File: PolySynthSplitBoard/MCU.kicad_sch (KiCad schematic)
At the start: 101 parts, among them J401 PWR, J402 DATA, J403 SWD Header, J404 MIDI_In, J405 Micro_SD_Card_Det2, J406 MIDI_Out, J407 MIDI_Thru, SW401 RST, SW402 BOOT, U401 STM32F411RETx, U402 74HC595, U403 74HC595, U404 74HC04, U405 6N138, Y401 16MHz, Y402 32.768kHZ

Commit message: voice rev4 passing DRC
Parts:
- added R447: LOOP, Resistor_THT:R_Axial_DIN0204_L3.6mm_D1.6mm_P5.08mm_Horizontal, symbol Device:R_US
- added TP421: INTR_A, TestPoint:TestPoint_THTPad_D1.0mm_Drill0.5mm_VAL, symbol Connector:TestPoint
- added TP422: INTR_B, TestPoint:TestPoint_THTPad_D1.0mm_Drill0.5mm_VAL, symbol Connector:TestPoint
- added TP423: INTR_C, TestPoint:TestPoint_THTPad_D1.0mm_Drill0.5mm_VAL, symbol Connector:TestPoint
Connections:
- net EXP_INTR_A: now also TP421.1
- net EXP_INTR_B: now also TP422.1
- net EXP_INTR_C: now also TP423.1
- net GND: now also R447.1, R447.2
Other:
- moved on the sheet: R446, TP418, TP419, TP420

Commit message: mod matrix logic stuff
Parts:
- TP401: value MUX_INH -> TestPoint; now left out of the parts list
- TP402: value MUX_A0 -> TestPoint; now left out of the parts list
- TP403: value MUX_A1 -> TestPoint; now left out of the parts list
- TP404: value MUX_A2 -> TestPoint; now left out of the parts list
- TP405: value HP_MODE -> TestPoint; now left out of the parts list
- TP406: value FOLD_FIRST -> TestPoint; now left out of the parts list
- TP407: value EXP_CS -> TestPoint; now left out of the parts list
- TP408: value EXP_SCK -> TestPoint; now left out of the parts list
- TP409: value EXP_MISO -> TestPoint; now left out of the parts list
- TP410: value EXP_MOSI -> TestPoint; now left out of the parts list
- TP411: value CLK_CS -> TestPoint; now left out of the parts list
- TP412: value CLK_SCK -> TestPoint; now left out of the parts list
- TP413: value CLK_MOSI -> TestPoint; now left out of the parts list
- TP414: value MIDI_RX -> TestPoint; now left out of the parts list
- TP415: value MIDI_TX -> TestPoint; now left out of the parts list
- TP416: value POTS_SCL -> TestPoint; now left out of the parts list
- TP417: value POTS_SDA -> TestPoint; now left out of the parts list
- TP418: value DAC_SCL -> TestPoint; now left out of the parts list
- TP419: value DAC_SDA -> TestPoint; now left out of the parts list
- TP420: value LDAC -> TestPoint; now left out of the parts list
- TP421: value INTR_A -> TestPoint; now left out of the parts list
- TP422: value INTR_B -> TestPoint; now left out of the parts list
- TP423: value INTR_C -> TestPoint; now left out of the parts list
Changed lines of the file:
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@@
 		(unit 1)
 		(exclude_from_sim no)
-		(in_bom yes)
+		(in_bom no)
 		(on_board yes)
 		(dnp no)
 		(fields_autoplaced yes)
 		(property "Reference" "TP403"
-			(at 83.058 236.4739 0)
+			(at 82.55 236.4739 0)
 			(effects
 				(font
@@
 			)
 		)
-		(property "Value" "MUX_A1"
-			(at 83.058 239.0139 0)
+		(property "Value" "TestPoint"
+			(at 82.55 239.0139 0)
 			(effects
 				(font
@@
 		(unit 1)
 		(exclude_from_sim no)
-		(in_bom yes)
+		(in_bom no)
 		(on_board yes)
 		(dnp no)
 		(fields_autoplaced yes)
 		(property "Reference" "TP423"
-			(at 188.722 247.3959 0)
+			(at 187.96 247.3959 0)
 			(effects
 				(font
@@
 			)
 		)
-		(property "Value" "INTR_C"
-			(at 188.722 249.9359 0)
+		(property "Value" "TestPoint"
+			(at 187.96 249.9359 0)
 			(effects
 				(font
@@
 		(unit 1)
 		(exclude_from_sim no)
-		(in_bom yes)
+		(in_bom no)
 		(on_board yes)
 		(dnp no)
 		(fields_autoplaced yes)
 		(property "Reference" "TP402"
-			(at 83.058 228.8539 0)
+			(at 83.82 228.8539 0)
 			(effects
 				(font
@@
 			)
 		)
-		(property "Value" "MUX_A0"
-			(at 83.058 231.3939 0)
+		(property "Value" "TestPoint"
+			(at 83.82 231.3939 0)
 			(effects
 				(font
@@
 		(unit 1)
 		(exclude_from_sim no)
-		(in_bom yes)
+		(in_bom no)
 		(on_board yes)
 		(dnp no)
@@
 			)
 		)
-		(property "Value" "EXP_SCK"
+		(property "Value" "TestPoint"
 			(at 118.11 242.5699 0)
 			(effects
@@
 		(unit 1)
 		(exclude_from_sim no)
-		(in_bom yes)
+		(in_bom no)
 		(on_board yes)
 		(dnp no)
 		(fields_autoplaced yes)
 		(property "Reference" "TP420"
-			(at 172.466 226.8219 0)
+			(at 172.72 226.8219 0)
 			(effects
 				(font
@@
 			)
 		)
-		(property "Value" "LDAC"
-			(at 172.466 229.3619 0)
+		(property "Value" "TestPoint"
+			(at 172.72 229.3619 0)
 			(effects
 				(font
@@
 		(unit 1)
 		(exclude_from_sim no)
-		(in_bom yes)
+		(in_bom no)
 		(on_board yes)
 		(dnp no)
 		(fields_autoplaced yes)
 		(property "Reference" "TP406"
-			(at 83.058 262.3819 0)
+			(at 83.82 262.3819 0)
 			(effects
 				(font
@@
 			)
 		)
-		(property "Value" "FOLD_FIRST"
-			(at 83.058 264.9219 0)
+		(property "Value" "TestPoint"
+			(at 83.82 264.9219 0)
 			(effects
 				(font
@@
 		(unit 1)
 		(exclude_from_sim no)
-		(in_bom yes)
+		(in_bom no)
 		(on_board yes)
 		(dnp no)
 		(fields_autoplaced yes)
 		(property "Reference" "TP422"
-			(at 187.452 235.4579 0)
+			(at 187.96 235.4579 0)
 			(effects
 				(font
@@
 			)
 		)
-		(property "Value" "INTR_B"
-			(at 187.452 237.9979 0)
+		(property "Value" "TestPoint"
+			(at 187.96 237.9979 0)
 			(effects
 				(font
@@
 		(unit 1)
 		(exclude_from_sim no)
-		(in_bom yes)
+		(in_bom no)
 		(on_board yes)
 		(dnp no)
 		(fields_autoplaced yes)
 		(property "Reference" "TP401"
-			(at 83.058 221.2339 0)
+			(at 83.82 221.2339 0)
 			(effects
 				(font
@@
 			)
 		)
-		(property "Value" "MUX_INH"
-			(at 83.058 223.7739 0)
+		(property "Value" "TestPoint"
+			(at 83.82 223.7739 0)
 			(effects
 				(font
@@
 		(unit 1)
 		(exclude_from_sim no)
-		(in_bom yes)
+		(in_bom no)
 		(on_board yes)
 		(dnp no)
 		(fields_autoplaced yes)
 		(property "Reference" "TP405"
-			(at 84.328 253.7459 0)
+			(at 83.82 253.7459 0)
 			(effects
 				(font
@@
 			)
 		)
-		(property "Value" "HP_MODE"
-			(at 84.328 256.2859 0)
+		(property "Value" "TestPoint"
+			(at 83.82 256.2859 0)
 			(effects
 				(font
@@
 		(unit 1)
 		(exclude_from_sim no)
-		(in_bom yes)
+		(in_bom no)
 		(on_board yes)
 		(dnp no)
@@
 			)
 		)
-		(property "Value" "POTS_SDA"
+		(property "Value" "TestPoint"
 			(at 154.94 227.5839 0)
 			(effects
@@
 		(unit 1)
 		(exclude_from_sim no)
-		(in_bom yes)
+		(in_bom no)
 		(on_board yes)
 		(dnp no)
@@
 			)
 		)
-		(property "Value" "EXP_MISO"
+		(property "Value" "TestPoint"
 			(at 118.11 252.4759 0)
 			(effects
@@
 		(unit 1)
 		(exclude_from_sim no)
-		(in_bom yes)
+		(in_bom no)
 		(on_board yes)
 		(dnp no)
 		(fields_autoplaced yes)
 		(property "Reference" "TP419"
-			(at 172.466 248.1579 0)
+			(at 172.72 248.1579 0)
 			(effects
 				(font
@@
 			)
 		)
-		(property "Value" "DAC_SDA"
-			(at 172.466 250.6979 0)
+		(property "Value" "TestPoint"
+			(at 172.72 250.6979 0)
 			(effects
 				(font
@@
 		(unit 1)
 		(exclude_from_sim no)
-		(in_bom yes)
+		(in_bom no)
 		(on_board yes)
 		(dnp no)
 		(fields_autoplaced yes)
 		(property "Reference" "TP413"
-			(at 137.922 257.5559 0)
+			(at 138.43 257.5559 0)
 			(effects
 				(font
@@
 			)
 		)
-		(property "Value" "CLK_MOSI"
-			(at 137.922 260.0959 0)
+		(property "Value" "TestPoint"
+			(at 138.43 260.0959 0)
 			(effects
 				(font
@@
 		(unit 1)
 		(exclude_from_sim no)
-		(in_bom yes)
+		(in_bom no)
 		(on_board yes)
 		(dnp no)
 		(fields_autoplaced yes)
 		(property "Reference" "TP421"
-			(at 187.452 219.9639 0)
+			(at 187.96 219.9639 0)
 			(effects
 				(font
@@
 			)
 		)
-		(property "Value" "INTR_A"
-			(at 187.452 222.5039 0)
+		(property "Value" "TestPoint"
+			(at 187.96 222.5039 0)
 			(effects
 				(font
@@
 		(unit 1)
 		(exclude_from_sim no)
-		(in_bom yes)
+		(in_bom no)
 		(on_board yes)
 		(dnp no)
 		(fields_autoplaced yes)
 		(property "Reference" "TP412"
-			(at 137.922 245.8719 0)
+			(at 138.43 245.8719 0)
 			(effects
 				(font
@@
 			)
 		)
-		(property "Value" "CLK_SCK"
-			(at 137.922 248.4119 0)
+		(property "Value" "TestPoint"
+			(at 138.43 248.4119 0)
 			(effects
 				(font
@@
 		(unit 1)
 		(exclude_from_sim no)
-		(in_bom yes)
+		(in_bom no)
 		(on_board yes)
 		(dnp no)
@@
 			)
 		)
-		(property "Value" "EXP_CS"
+		(property "Value" "TestPoint"
 			(at 118.11 232.9179 0)
 			(effects
@@
 		(unit 1)
 		(exclude_from_sim no)
-		(in_bom yes)
+		(in_bom no)
 		(on_board yes)
 		(dnp no)
 		(fields_autoplaced yes)
 		(property "Reference" "TP404"
-			(at 83.058 244.6019 0)
+			(at 83.82 244.6019 0)
 			(effects
 				(font
@@
 			)
 		)
-		(property "Value" "MUX_A2"
-			(at 83.058 247.1419 0)
+		(property "Value" "TestPoint"
+			(at 83.82 247.1419 0)
 			(effects
 				(font
@@
 		(unit 1)
 		(exclude_from_sim no)
-		(in_bom yes)
+		(in_bom no)
 		(on_board yes)
 		(dnp no)
 		(fields_autoplaced yes)
 		(property "Reference" "TP411"
-			(at 137.922 236.4739 0)
+			(at 137.16 236.4739 0)
 			(effects
 				(font
@@
 			)
 		)
-		(property "Value" "CLK_CS"
-			(at 137.922 239.0139 0)
+		(property "Value" "TestPoint"
+			(at 137.16 239.0139 0)
 			(effects
 				(font
@@
 		(unit 1)
 		(exclude_from_sim no)
-		(in_bom yes)
+		(in_bom no)
 		(on_board yes)
 		(dnp no)
@@
 			)
 		)
-		(property "Value" "EXP_MOSI"
+		(property "Value" "TestPoint"
 			(at 118.11 262.3819 0)
 			(effects
@@
 		(unit 1)
 		(exclude_from_sim no)
-		(in_bom yes)
+		(in_bom no)
 		(on_board yes)
 		(dnp no)
@@
 			)
 		)
-		(property "Value" "MIDI_TX"
+		(property "Value" "TestPoint"
 			(at 137.16 227.8379 0)
 			(effects
@@
 		(unit 1)
 		(exclude_from_sim no)
-		(in_bom yes)
+		(in_bom no)
 		(on_board yes)
 		(dnp no)
@@
 			)
 		)
-		(property "Value" "POTS_SCL"
+		(property "Value" "TestPoint"
 			(at 153.67 217.9319 0)
 			(effects
@@
 		(unit 1)
 		(exclude_from_sim no)
-		(in_bom yes)
+		(in_bom no)
 		(on_board yes)
 		(dnp no)
 		(fields_autoplaced yes)
 		(property "Reference" "TP418"
-			(at 172.466 237.4899 0)
+			(at 172.72 237.4899 0)
 			(effects
 				(font
@@
 			)
 		)
-		(property "Value" "DAC_SCL"
-			(at 172.466 240.0299 0)
+		(property "Value" "TestPoint"
+			(at 172.72 240.0299 0)
 			(effects
 				(font
@@
 		(unit 1)
 		(exclude_from_sim no)
-		(in_bom yes)
+		(in_bom no)
 		(on_board yes)
 		(dnp no)
@@
 			)
 		)
-		(property "Value" "MIDI_RX"
+		(property "Value" "TestPoint"
 			(at 137.16 217.6779 0)
 			(effects

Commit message: motherboard rev2 passing DRC
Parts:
- TP401: value TestPoint -> MUX_INH
- TP402: value TestPoint -> MUX_A0
- TP403: value TestPoint -> MUX_A1
- TP404: value TestPoint -> MUX_A2
- TP405: value TestPoint -> HP_MODE
- TP406: value TestPoint -> FF
- TP407: value TestPoint -> EXP_CS
- TP408: value TestPoint -> EXP_SCK
- TP409: value TestPoint -> EXP_MISO
- TP410: value TestPoint -> EXP_MOSI
- TP411: value TestPoint -> PITCH_SS
- TP412: value TestPoint -> PITCH_SCK
- TP413: value TestPoint -> PITCH_MOSI
- TP414: value TestPoint -> MIDI_R
- TP415: value TestPoint -> MIDI_T
- TP416: value TestPoint -> POTS_SCL
- TP417: value TestPoint -> POTS_SDA
- TP418: value TestPoint -> DAC_SCL
- TP419: value TestPoint -> DAC_SDA
- TP420: value TestPoint -> LDAC
- TP421: value TestPoint -> EXP_INTA
- TP422: value TestPoint -> EXP_INTB
- TP423: value TestPoint -> EXP_INTC
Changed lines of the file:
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@@
 			)
 		)
-		(property "Value" "TestPoint"
+		(property "Value" "MUX_A1"
 			(at 82.55 239.0139 0)
 			(effects
@@
 			)
 		)
-		(property "Value" "TestPoint"
+		(property "Value" "EXP_INTC"
 			(at 187.96 249.9359 0)
 			(effects
@@
 			)
 		)
-		(property "Value" "TestPoint"
+		(property "Value" "MUX_A0"
 			(at 83.82 231.3939 0)
 			(effects
@@
 			)
 		)
-		(property "Value" "TestPoint"
+		(property "Value" "EXP_SCK"
 			(at 118.11 242.5699 0)
 			(effects
@@
 			)
 		)
-		(property "Value" "TestPoint"
+		(property "Value" "LDAC"
 			(at 172.72 229.3619 0)
 			(effects
@@
 			)
 		)
-		(property "Value" "TestPoint"
+		(property "Value" "FF"
 			(at 83.82 264.9219 0)
 			(effects
@@
 			)
 		)
-		(property "Value" "TestPoint"
+		(property "Value" "EXP_INTB"
 			(at 187.96 237.9979 0)
 			(effects
@@
 			)
 		)
-		(property "Value" "TestPoint"
+		(property "Value" "MUX_INH"
 			(at 83.82 223.7739 0)
 			(effects
@@
 			)
 		)
-		(property "Value" "TestPoint"
+		(property "Value" "HP_MODE"
 			(at 83.82 256.2859 0)
 			(effects
@@
 			)
 		)
-		(property "Value" "TestPoint"
+		(property "Value" "POTS_SDA"
 			(at 154.94 227.5839 0)
 			(effects
@@
 			)
 		)
-		(property "Value" "TestPoint"
+		(property "Value" "EXP_MISO"
 			(at 118.11 252.4759 0)
 			(effects
@@
 			)
 		)
-		(property "Value" "TestPoint"
+		(property "Value" "DAC_SDA"
 			(at 172.72 250.6979 0)
 			(effects
@@
 			)
 		)
-		(property "Value" "TestPoint"
+		(property "Value" "PITCH_MOSI"
 			(at 138.43 260.0959 0)
 			(effects
@@
 			)
 		)
-		(property "Value" "TestPoint"
+		(property "Value" "EXP_INTA"
 			(at 187.96 222.5039 0)
 			(effects
@@
 			)
 		)
-		(property "Value" "TestPoint"
+		(property "Value" "PITCH_SCK"
 			(at 138.43 248.4119 0)
 			(effects
@@
 			)
 		)
-		(property "Value" "TestPoint"
+		(property "Value" "EXP_CS"
 			(at 118.11 232.9179 0)
 			(effects
@@
 			)
 		)
-		(property "Value" "TestPoint"
+		(property "Value" "MUX_A2"
 			(at 83.82 247.1419 0)
 			(effects
@@
 			)
 		)
-		(property "Value" "TestPoint"
+		(property "Value" "PITCH_SS"
 			(at 137.16 239.0139 0)
 			(effects
@@
 			)
 		)
-		(property "Value" "TestPoint"
+		(property "Value" "EXP_MOSI"
 			(at 118.11 262.3819 0)
 			(effects
@@
 			)
 		)
-		(property "Value" "TestPoint"
+		(property "Value" "MIDI_T"
 			(at 137.16 227.8379 0)
 			(effects
@@
 			)
 		)
-		(property "Value" "TestPoint"
+		(property "Value" "POTS_SCL"
 			(at 153.67 217.9319 0)
 			(effects
@@
 			)
 		)
-		(property "Value" "TestPoint"
+		(property "Value" "DAC_SCL"
 			(at 172.72 240.0299 0)
 			(effects
@@
 			)
 		)
-		(property "Value" "TestPoint"
+		(property "Value" "MIDI_R"
 			(at 137.16 217.6779 0)
 			(effects

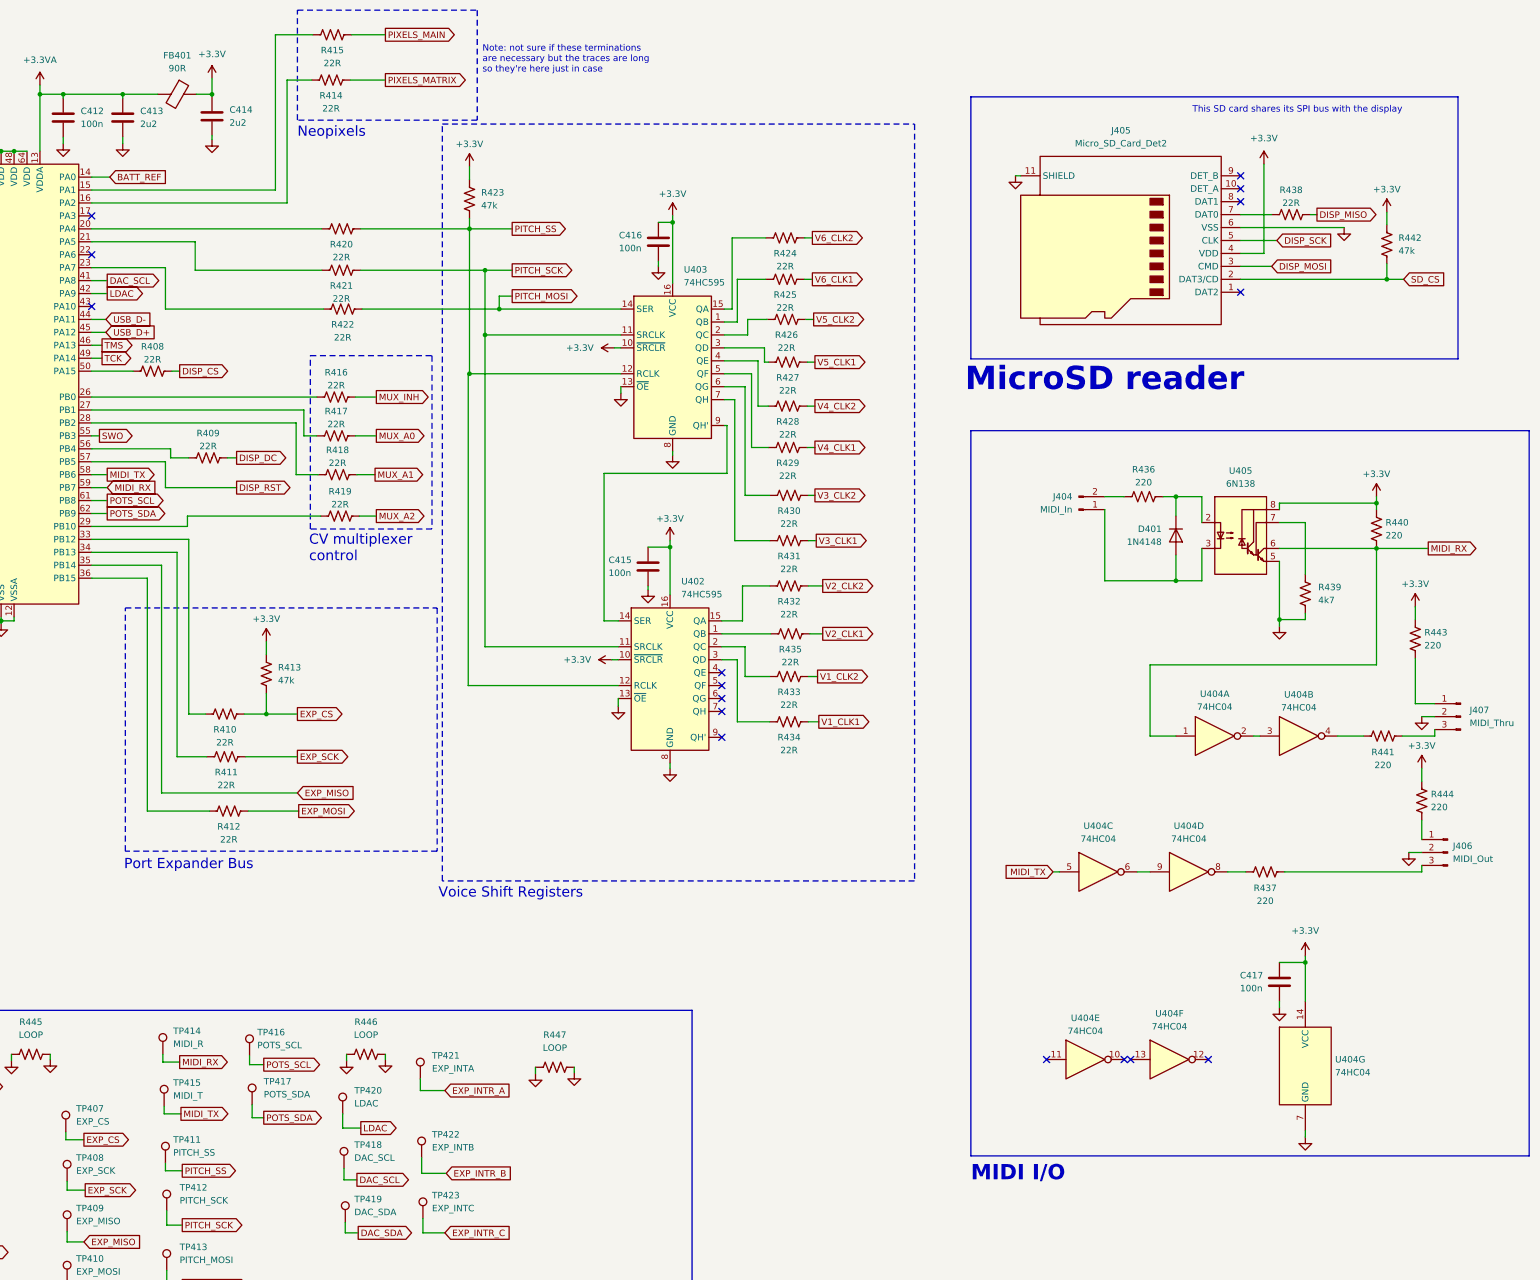
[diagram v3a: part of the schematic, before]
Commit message: hardware chip select for pitch registers
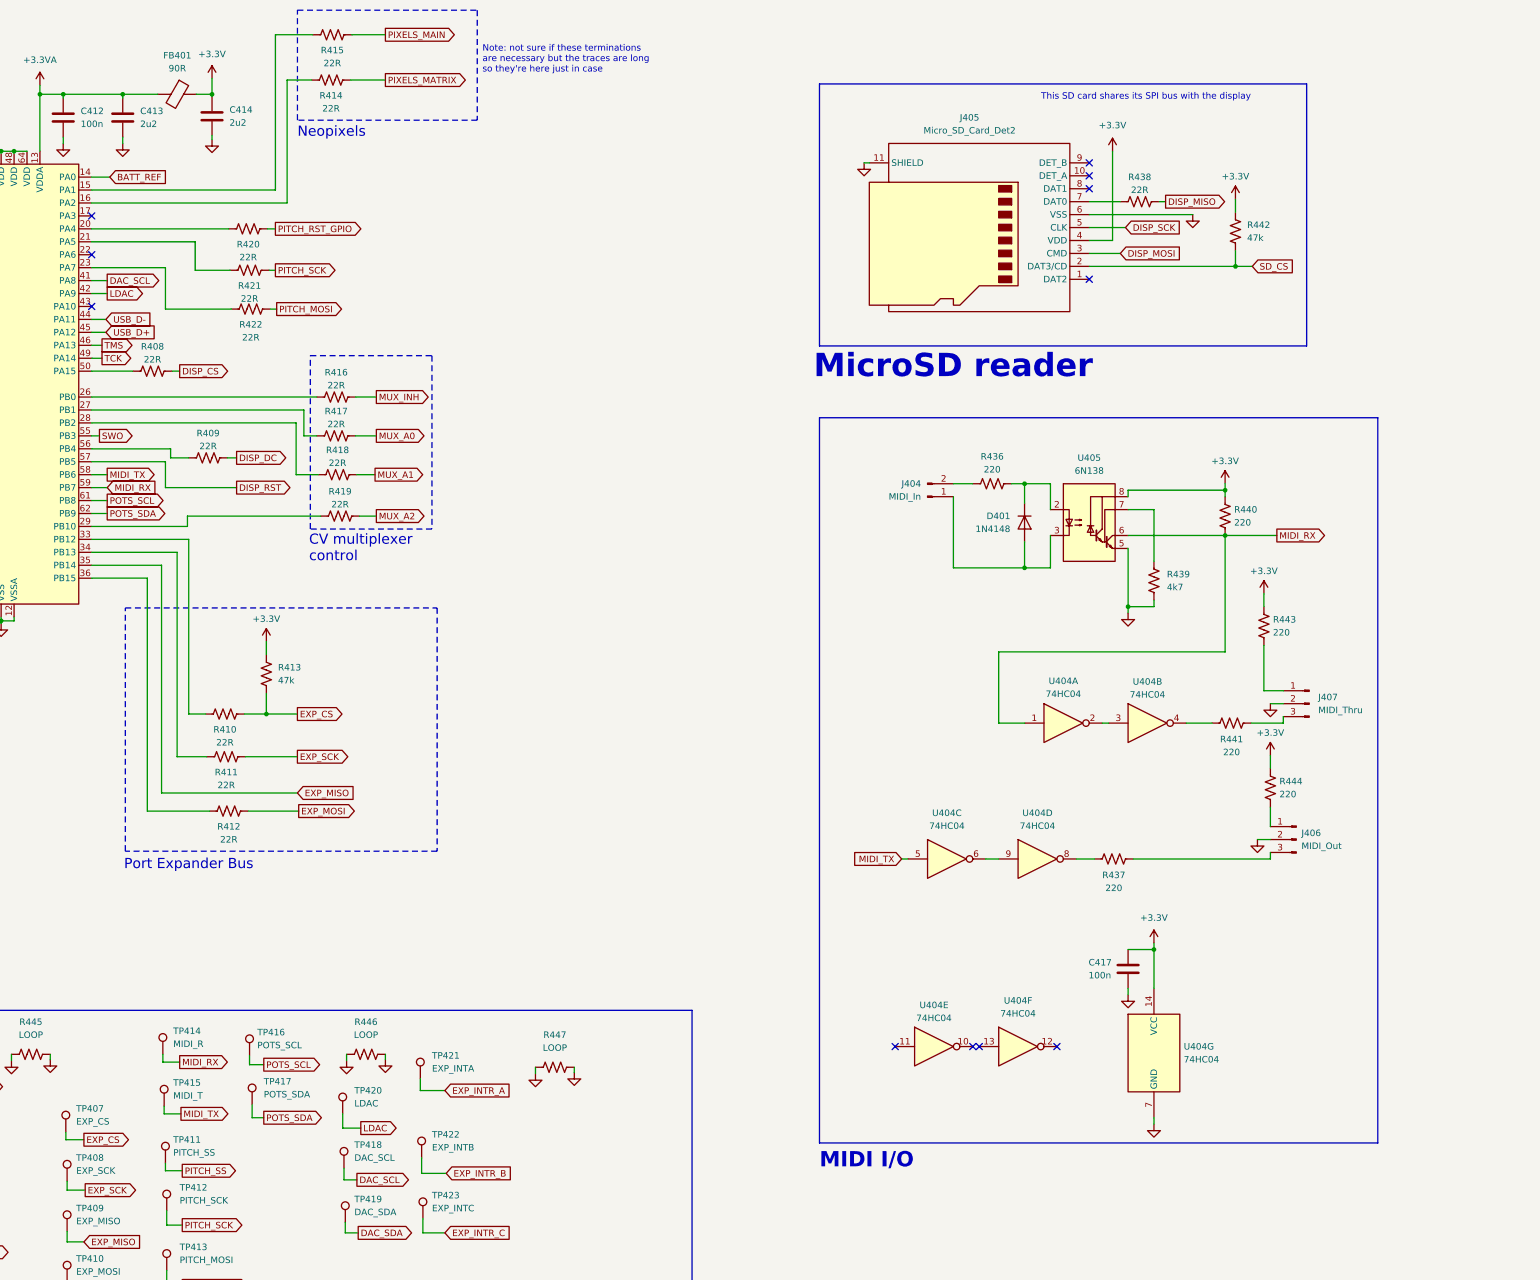
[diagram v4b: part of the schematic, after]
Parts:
- removed C415, C416: 100n, Capacitor_SMD:C_0805_2012Metric, symbol Device:C
- removed R423: 47k, Resistor_SMD:R_0805_2012Metric, symbol Device:R_US
- removed R424, R425, R426, R427, R428, R429, R430, R431, R432, R433, R434, R435: 22R, Resistor_SMD:R_0805_2012Metric, symbol Device:R_US
- removed U402, U403: 74HC595, Package_SO:SOIC-16_3.9x9.9mm_P1.27mm, symbol 74xx:74HC595
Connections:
- net PITCH_SS: no longer R420.2
- new net PITCH_RST_GPIO: R420.2
- no-connect marks 21 -> 16
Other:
- note removed: "Voice Shift Registers"
- moved on the sheet: C417, D401, J404, J405, J406, J407, R421, R422, R436, R437, R438, R439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

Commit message: hardware CS stuff passing DRC
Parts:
- TP411: value PITCH_SS -> P_RST_GPIO
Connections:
- net PITCH_SS is gone; now on net PITCH_RST_GPIO: TP411.1
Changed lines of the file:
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@@
 		)
 	)
-	(global_label "PITCH_SS"
+	(global_label "PITCH_RST_GPIO"
 		(shape output)
 		(at 138.938 242.57 0)
@@
 		)
 		(property "Intersheetrefs" "${INTERSHEET_REFS}"
-			(at 150.7527 242.57 0)
+			(at 157.2237 242.57 0)
 			(effects
 				(font
@@
 			)
 		)
-		(property "Value" "PITCH_SS"
+		(property "Value" "P_RST_GPIO"
 			(at 137.16 239.0139 0)
 			(effects
